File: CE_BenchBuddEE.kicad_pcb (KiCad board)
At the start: 4 copper layers, 165.1 x 63.5 mm, 31 parts, among them K1 1461069-5, P1 CONN_2, P2 CONN_3X2, Q1 2N3904, U1 MCP3901, U2 OPA4170, U3 LMT84, U4 LTV-816S

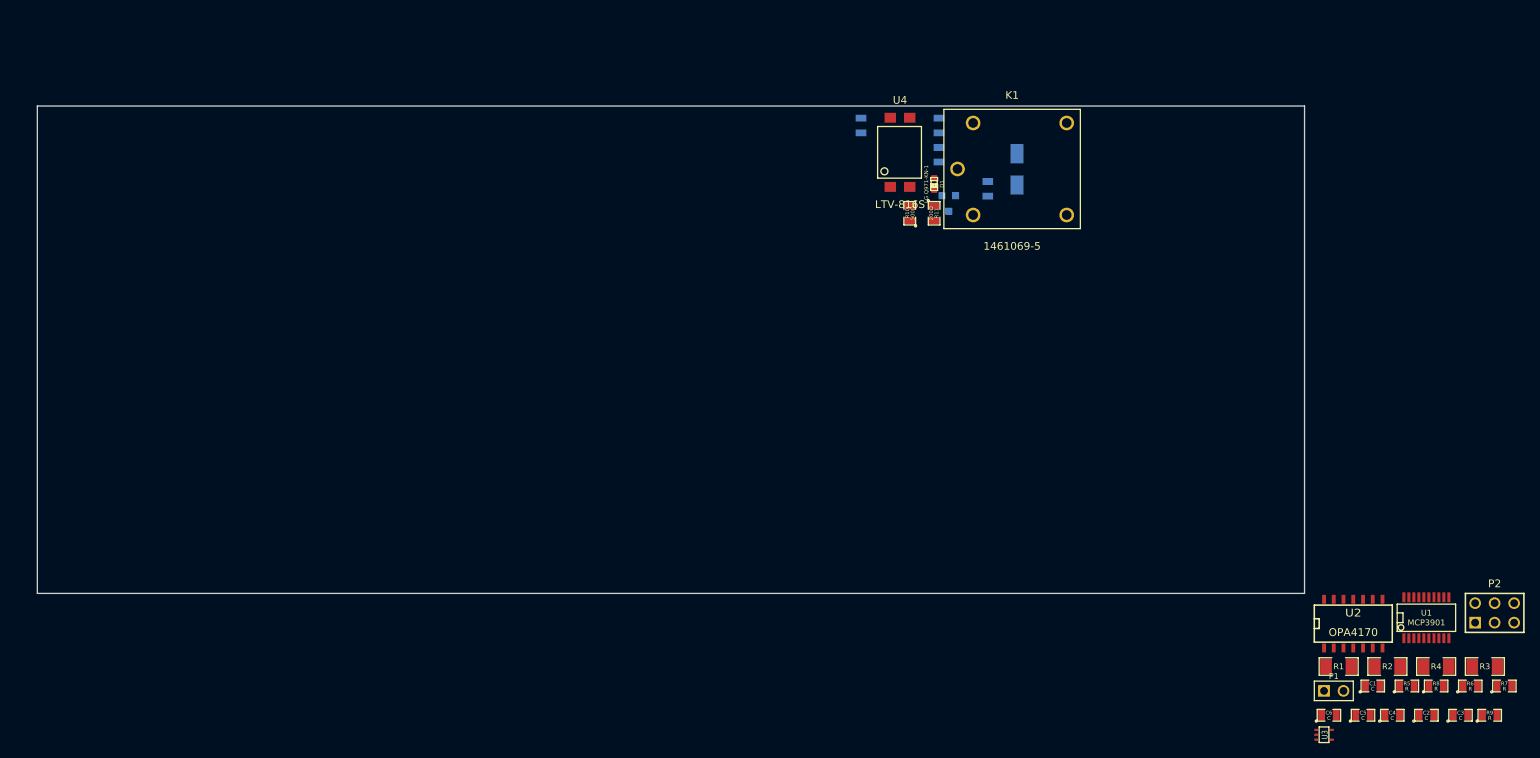
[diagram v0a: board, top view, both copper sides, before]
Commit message: Initial layout of Arduino and Fan-Current
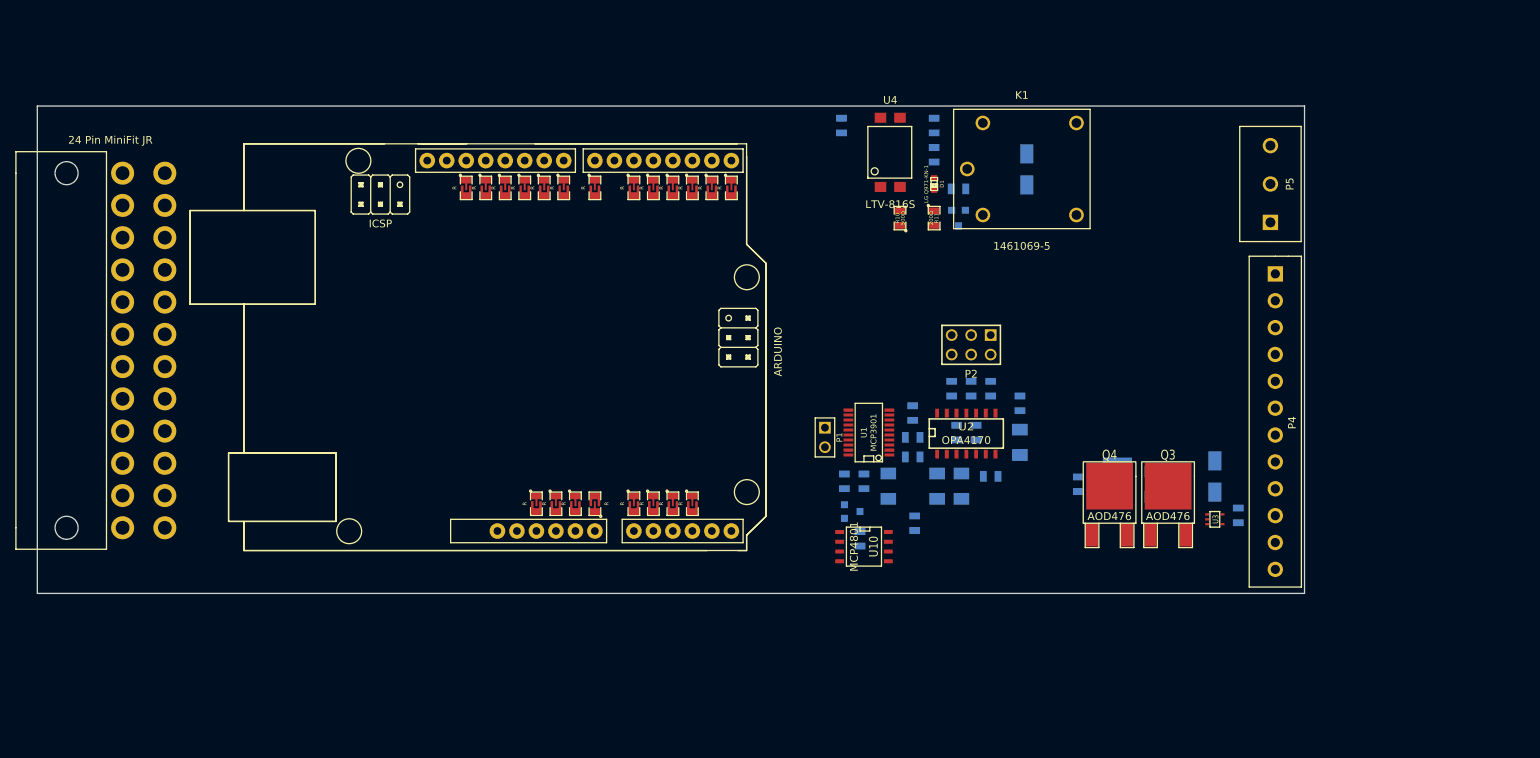
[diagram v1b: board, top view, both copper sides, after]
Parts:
- added ARD1: ARDUINO, Arduino_Uno_R3_Footprint, F.Cu at (217.4, 167.1)
- added C12: C, SM0805, B.Cu at (234.2, 168.1)
- added C13: C, SM0805, B.Cu at (262.6, 161.0)
- added D4: B130-13-F, SMA, B.Cu at (280.4, 160.0)
- added P3: 24 Pin MiniFit JR, ATX_Header, F.Cu at (130.8, 143.5)
- added P4: 12 Pin Terminal Block, 12_Pin_TB, F.Cu at (288.3, 151.1)
- added P5: 3 Pin TB, 3_Pin_TB, F.Cu at (287.7, 121.9)
- added Q2: DMN65D8L-7, SOT23GDS, B.Cu at (233.2, 164.6)
- added Q3: AOD476, DPAK2, F.Cu at (274.3, 167.6)
- added Q4: AOD476, DPAK2, F.Cu at (266.7, 167.6)
- added R26: R, SM0805, B.Cu at (241.3, 166.1)
- added R27: R, SM1206, B.Cu at (272.3, 161.0)
- added R28: R, SM0805-BRIDGE, F.Cu at (192.0, 163.6)
- added R29: R, SM0805-BRIDGE, F.Cu at (199.6, 163.6)
- added R30: R, SM0805-BRIDGE, F.Cu at (204.7, 163.6)
- added R31: R, SM0805-BRIDGE, F.Cu at (207.3, 163.6)
- added R32: R, SM0805-BRIDGE, F.Cu at (209.8, 163.6)
- added R33: R, SM0805-BRIDGE, F.Cu at (212.3, 163.6)
- added R34: R, SM0805-BRIDGE, F.Cu at (182.9, 122.4)
- added R35: R, SM0805-BRIDGE, F.Cu at (185.4, 122.4)
- added R36: R, SM0805-BRIDGE, F.Cu at (188.0, 122.4)
- added R37: R, SM0805-BRIDGE, F.Cu at (190.5, 122.4)
- added R38: R, SM0805-BRIDGE, F.Cu at (193.0, 122.4)
- added R39: R, SM0805-BRIDGE, F.Cu at (195.6, 122.4)
- added R40: R, SM0805-BRIDGE, F.Cu at (199.6, 122.4)
- added R41: R, SM0805-BRIDGE, F.Cu at (204.7, 122.4)
- added R42: R, SM0805-BRIDGE, F.Cu at (207.3, 122.4)
- added R43: R, SM0805-BRIDGE, F.Cu at (214.9, 122.4)
- added R44: R, SM0805-BRIDGE, F.Cu at (217.4, 122.4)
- added R46: 0Ω, SM0805, B.Cu at (232.2, 160.7)
- added R47: 0Ω, SM0805, B.Cu at (234.7, 160.7)
- added R48: R, SM0805-BRIDGE, F.Cu at (194.6, 163.6)
- added R49: R, SM0805-BRIDGE, F.Cu at (197.1, 163.6)
- added R50: R, SM0805-BRIDGE, F.Cu at (209.8, 122.4)
- added R51: R, SM0805-BRIDGE, F.Cu at (212.3, 122.4)
- added TH5: MINISMDC050F-2, SM1812, B.Cu at (267.7, 160.5)
- added U10: MCP4801, SO8N, F.Cu at (234.7, 169.2)
- C1, C2, C3, C4, C5, C6, R1, R2, R3, R4, R5, R6, R7, R8, R9: moved to B.Cu
- U2: footprint SO14N -> SO14E
- moved R7 81.8 mm to (246.1, 148.6), turned to 270 degrees
- moved C3 81.5 mm to (241.0, 151.8), turned to 90 degrees
- moved R9 77.7 mm to (251.2, 148.6), turned to 270 degrees
- moved P2 76.6 mm to (248.7, 142.9), turned to 180 degrees
- moved U1 76.5 mm to (235.3, 154.3), turned to 90 degrees
- moved C2 76.1 mm to (241.0, 154.9)
- moved P1 74.1 mm to (229.6, 154.9), turned to 270 degrees
- moved R8 71.9 mm to (248.7, 148.6), turned to 270 degrees
- moved R6 69.3 mm to (255.0, 150.5), turned to 270 degrees
- moved R3 67.3 mm to (255.0, 155.6), turned to 270 degrees
- moved C1 67.0 mm to (241.0, 157.5), turned to 180 degrees
- moved R4 66.2 mm to (247.4, 161.3), turned to 270 degrees
- moved C4 65.6 mm to (249.3, 154.3), turned to 90 degrees
- moved C5 64.5 mm to (246.8, 154.3), turned to 270 degrees
- moved R1 63.2 mm to (237.9, 161.3), turned to 270 degrees
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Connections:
- C3 pad 1: N-0000079 (its old number) -> /Thermocouple/CH0+
- C3 pad 2: AGND -> /Thermocouple/CH0-
- K1 pad 1: (no net) -> /Relay/RELAY_COM
- K1 pad 3: (no net) -> /Relay/RELAY_NO
- K1 pad 4: (no net) -> /Terminal Block/RELAY_COM
- R1 pad 1: N-0000079 (its old number) -> /Thermocouple/CH0+
- U1 pad 14: (no net) -> /Arduino/~DR
- U1 pad 4: N-0000079 (its old number) -> /Thermocouple/CH0+
- U1 pad 5: AGND -> /Thermocouple/CH0-
- U1 pad 6: AGND -> /Thermocouple/CH1-
- U1 pad 7: N-0000078 (its old number) -> /Thermocouple/CH1+
- U2 pad 1: N-0000079 (its old number) -> /Thermocouple/CH0+
- U2 pad 10: (no net) -> /Thermocouple/TC_IN -
- U2 pad 5: (no net) -> /Thermocouple/TC_IN +
- U3 pad 3: N-0000078 (its old number) -> /Thermocouple/CH1+

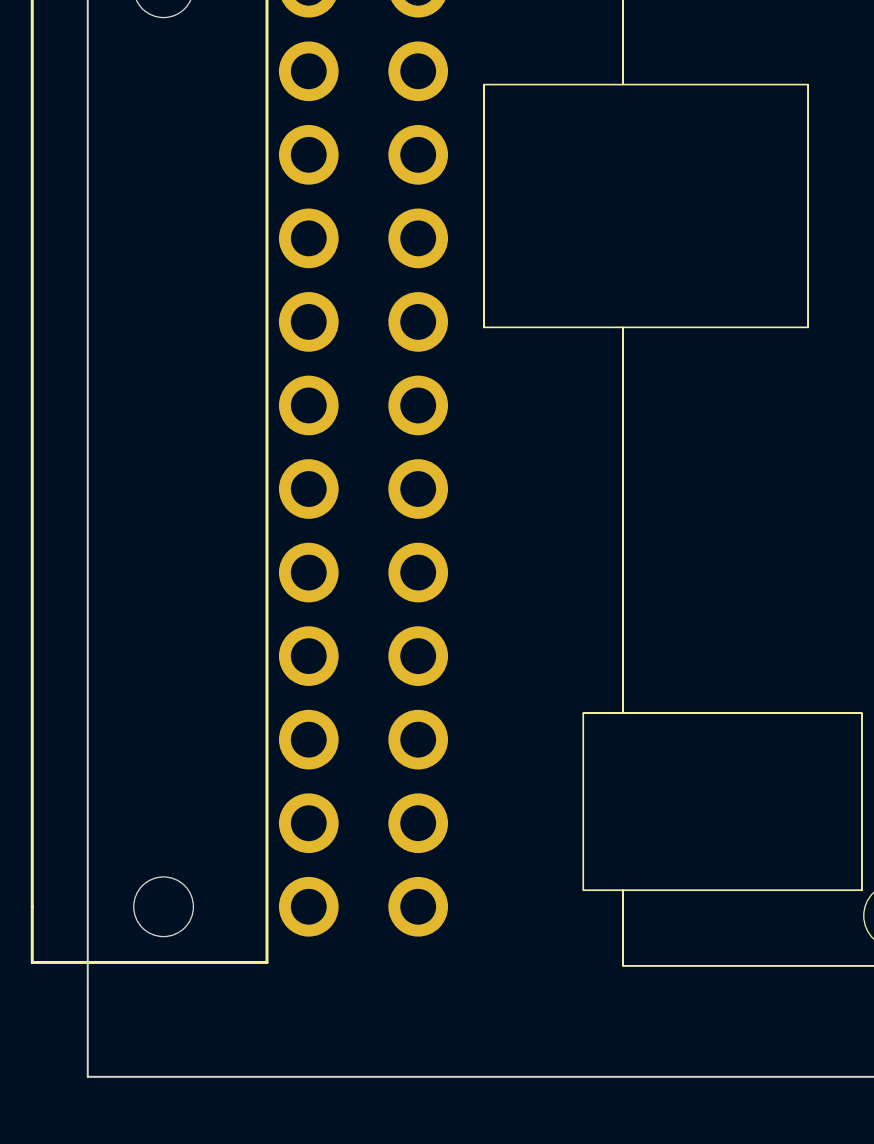
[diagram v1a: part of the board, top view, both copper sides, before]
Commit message: Reorganization of power conditioning module
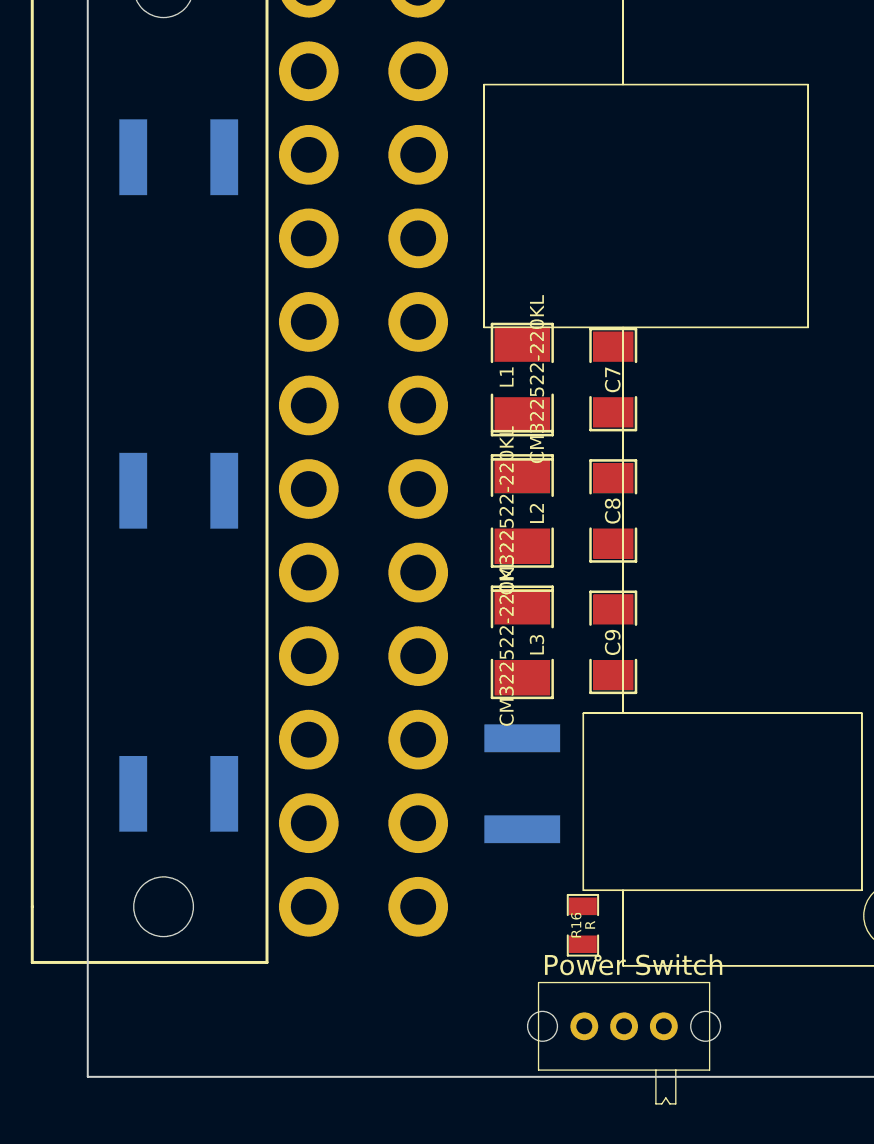
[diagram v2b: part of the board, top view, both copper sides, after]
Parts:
- added C7: C, SM1206, F.Cu at (153.4, 140.2)
- added C8: C, SM1206, F.Cu at (153.4, 146.8)
- added C9: C, SM1206, F.Cu at (153.4, 153.4)
- added L1: CM322522-220KL, SM1210L, F.Cu at (148.8, 140.2)
- added L2: CM322522-220KL, SM1210L, F.Cu at (148.8, 146.8)
- added L3: CM322522-220KL, SM1210L, F.Cu at (148.8, 153.4)
- added R16: R, SM0805, F.Cu at (151.9, 167.6)
- added SW1: Power Switch, BB_Switch, F.Cu at (149.9, 172.7)
- added TH1: MINISMDC050F-2, SM1812, B.Cu at (131.6, 161.0)
- added TH2: MINISMDC050F-2, SM1812, B.Cu at (131.6, 145.8)
- added TH3: MINISMDC050F-2, SM1812, B.Cu at (131.6, 129.0)
- added TH4: MINISMDC050F-2, SM1812, B.Cu at (148.8, 160.5)
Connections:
- R38 pad 2: (no net) -> /Arduino/LED_EN_PWM

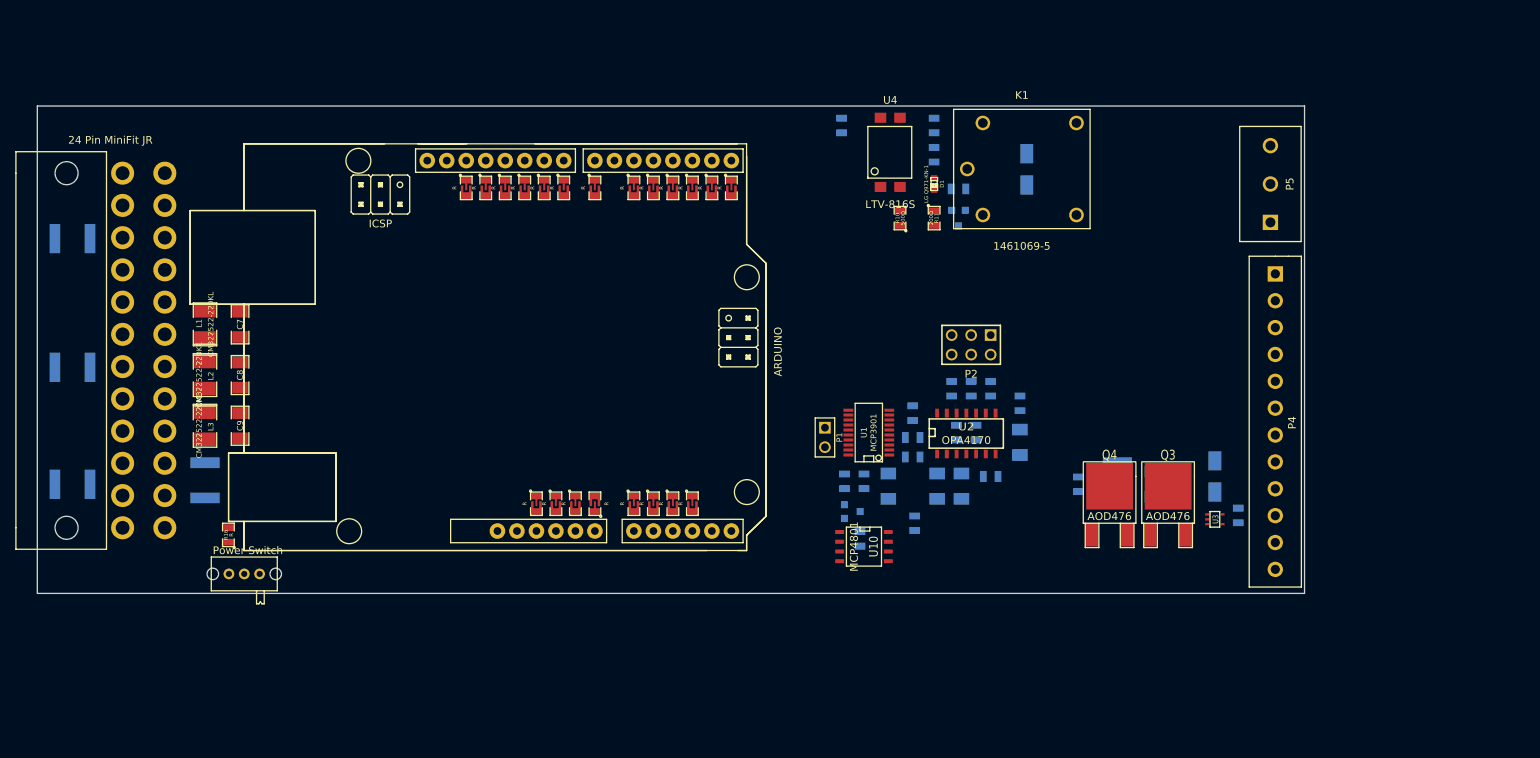
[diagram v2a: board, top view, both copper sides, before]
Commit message: Association and layout of the power regulator mod
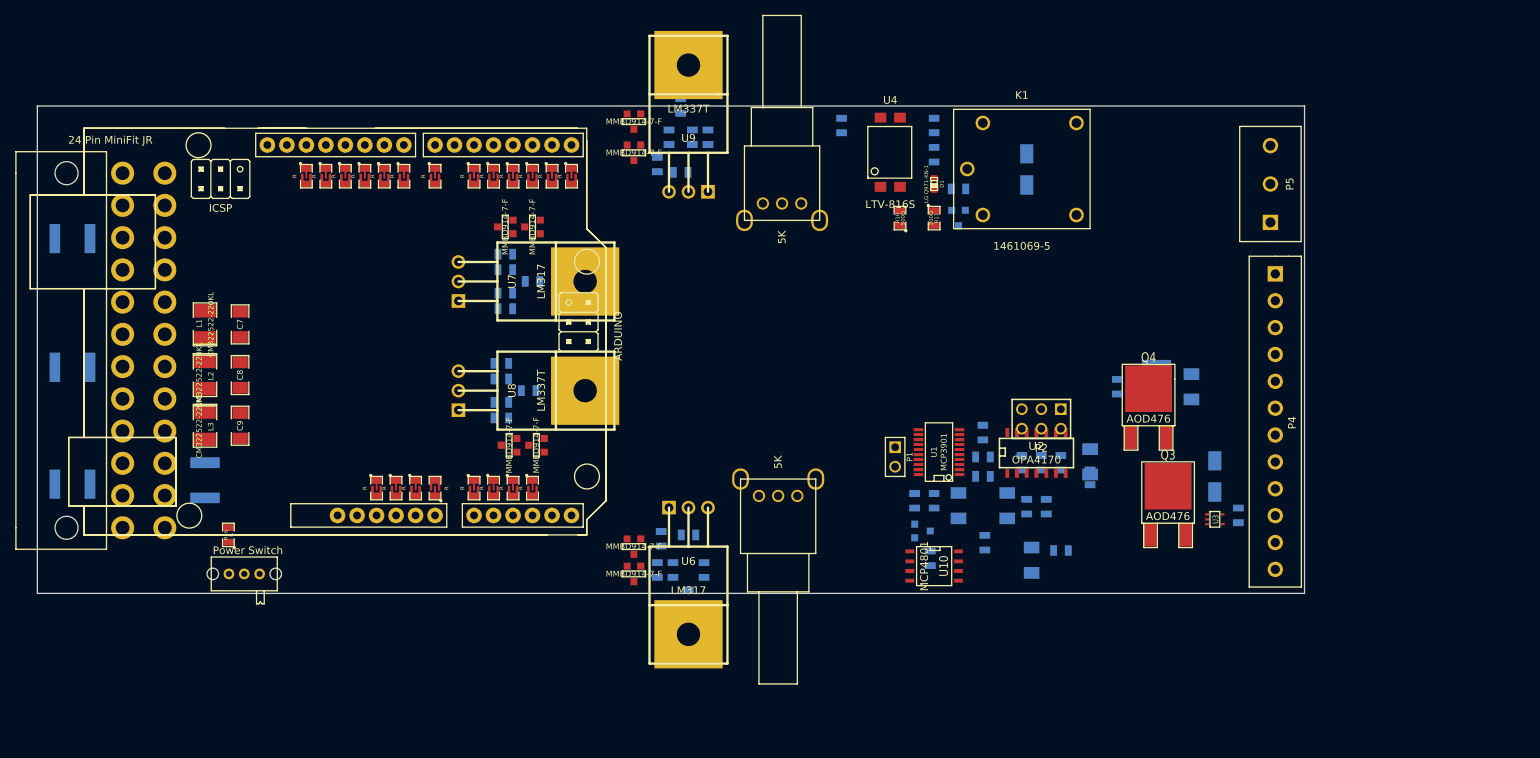
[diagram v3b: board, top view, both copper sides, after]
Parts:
- added C14: C, SM0805, B.Cu at (188.0, 138.2)
- added C15: C, SM0805, B.Cu at (187.5, 152.4)
- added C16: C, SM0805, B.Cu at (191.5, 134.6)
- added C17: C, SM0805, B.Cu at (191.0, 148.8)
- added C18: C, SM0805, B.Cu at (188.0, 136.1)
- added C19: C, SM0805, B.Cu at (187.5, 150.4)
- added C20: C, SM0805, B.Cu at (207.8, 172.2)
- added C21: C, SM0805, B.Cu at (214.4, 115.8)
- added C22: C, SM0805, B.Cu at (211.8, 175.8)
- added C23: C, SM0805, B.Cu at (210.8, 111.8)
- added C24: C, SM0805, B.Cu at (209.8, 172.2)
- added C25: C, SM0805, B.Cu at (212.3, 115.8)
- added D10: MMBD914-7-F, SOT23-DIODE, F.Cu at (204.7, 113.8)
- added D11: MMBD914-7-F, SOT23-DIODE, F.Cu at (204.7, 169.2)
- added D12: MMBD914-7-F, SOT23-DIODE, F.Cu at (204.7, 117.9)
- added D5: MMBD914-7-F, SOT23-DIODE, F.Cu at (191.5, 127.5)
- added D6: MMBD914-7-F, SOT23-DIODE, F.Cu at (192.0, 156.0)
- added D7: MMBD914-7-F, SOT23-DIODE, F.Cu at (188.0, 127.5)
- added D8: MMBD914-7-F, SOT23-DIODE, F.Cu at (188.5, 156.0)
- added D9: MMBD914-7-F, SOT23-DIODE, F.Cu at (204.7, 172.7)
- added R18: 5K, EVUE3K, F.Cu at (223.5, 162.6)
- added R19: 715Ω, SM0805, B.Cu at (213.9, 172.2)
- added R20: R, SM0805, B.Cu at (188.0, 133.1)
- added R21: R, SM0805, B.Cu at (187.5, 147.3)
- added R22: R, SM0805, B.Cu at (211.8, 167.6)
- added R23: R, SM0805, B.Cu at (208.3, 168.1)
- added R24: R, SM0805, B.Cu at (207.8, 119.4)
- added R25: R, SM0805, B.Cu at (210.8, 120.4)
- added R52: 5K, EVUE3K, F.Cu at (224.0, 124.5)
- added R53: R, SM0805, B.Cu at (187.5, 145.3)
- added R54: 715Ω, SM0805, B.Cu at (209.3, 115.8)
- added R55: R, SM0805, B.Cu at (188.0, 131.1)
- added U6: LM317, TO220, F.Cu at (211.8, 164.1)
- added U7: LM317, TO220, F.Cu at (181.9, 134.6)
- added U8: LM337T, TO220, F.Cu at (181.9, 148.8)
- added U9: LM337T, TO220, F.Cu at (211.8, 122.9)
- moved ARD1 20.9 mm to (196.6, 165.1)
- moved R28 20.9 mm to (171.2, 161.5)
- moved R29 20.9 mm to (178.8, 161.5)
- moved R30 20.9 mm to (183.9, 161.5)
- moved R31 20.9 mm to (186.4, 161.5)
- moved R32 20.9 mm to (189.0, 161.5)
- moved R33 20.9 mm to (191.5, 161.5)
- moved R48 20.9 mm to (173.7, 161.5)
- moved R49 20.9 mm to (176.3, 161.5)
- moved R34 20.9 mm to (162.1, 120.9)
- moved R36 20.9 mm to (167.1, 120.9)
- moved R37 20.9 mm to (169.7, 120.9)
- moved R38 20.9 mm to (172.2, 120.9)
- moved R39 20.9 mm to (174.8, 120.9)
- moved R40 20.9 mm to (178.8, 120.9)
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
